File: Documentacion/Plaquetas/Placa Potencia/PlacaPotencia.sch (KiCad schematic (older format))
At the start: 31 parts, among them J1 Conn_01x02_Male, Q1 IRF4905, Q2 IRFZ44N, Q3 IRF4905, Q4 IRFZ44N, Q5 BC337, Q6 BC337, U2 MCP1407, U3 MCP1407

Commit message: Possible layout
Needs some rearenging.
Added kiCAD backup files to ignore list
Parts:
- BORNERA2, BORNERA3: footprint TerminalBlock:TerminalBlock_bornier-2_P5.08mm -> Connector_PinHeader_2.54mm:PinHeader_1x02_P2.54mm_Vertical
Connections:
- net PMOS_CALOR: now also BORNERA3.1 (Pin_1); no longer BORNERA2.2 (Pin_2)
- net PWM_FRIO: now also BORNERA2.2 (Pin_2); no longer BORNERA3.1 (Pin_1)
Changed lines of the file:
@@
 EESchema Schematic File Version 4
+LIBS:PlacaPotencia-cache
 EELAYER 30 0
 EELAYER END
@@
 	1    0    0    -1
 $EndComp
-Text GLabel 9850 1550 2    50   Input ~ 0
+Text GLabel 9950 3100 2    50   Input ~ 0
 PMOS_CALOR
-Text GLabel 9850 1850 2    50   Input ~ 0
-PMOS_FRIO
 $Comp
 L Connector:Screw_Terminal_01x02 BORNERA1
@@
 F 0 "BORNERA2" V 9464 1562 50  0000 R CNN
 F 1 "Screw_Terminal_01x02" V 9373 1562 50  0000 R CNN
-F 2 "TerminalBlock:TerminalBlock_bornier-2_P5.08mm" H 9500 1750 50  0001 C CNN
+F 2 "Connector_PinHeader_2.54mm:PinHeader_1x02_P2.54mm_Vertical" H 9500 1750 50  0001 C CNN
 F 3 "~" H 9500 1750 50  0001 C CNN
 	1    9500 1750
@@
 F 0 "BORNERA3" V 9484 2822 50  0000 R CNN
 F 1 "Screw_Terminal_01x02" V 9393 2822 50  0000 R CNN
-F 2 "TerminalBlock:TerminalBlock_bornier-2_P5.08mm" H 9520 3010 50  0001 C CNN
+F 2 "Connector_PinHeader_2.54mm:PinHeader_1x02_P2.54mm_Vertical" H 9520 3010 50  0001 C CNN
 F 3 "~" H 9520 3010 50  0001 C CNN
 	1    9520 3010
 	-1   0    0    1
 $EndComp
-Text GLabel 9950 3100 2    50   Input ~ 0
-PWM_FRIO
 Text GLabel 9950 2800 2    50   Input ~ 0
 PWM_CALOR
@@
 Wire Wire Line
 	9850 2800 9950 2800
+NoConn ~ 10540 810
+NoConn ~ 10540 910
 $Comp
 L Connector:Conn_01x02_Male J1
@@
 	1    0    0    -1
 $EndComp
-NoConn ~ 10540 810
-NoConn ~ 10540 910
+Text GLabel 9850 1850 2    50   Input ~ 0
+PMOS_FRIO
+Text GLabel 9850 1550 2    50   Input ~ 0
+PWM_FRIO
 $EndSCHEMATC

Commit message: Power PCB Routed
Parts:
- added C_MCP1, C_MCP2: 10n, Capacitor_THT:C_Rect_L7.5mm_W6.5mm_P5.00mm, symbol Device:C
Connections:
- net GND: now also C_MCP1.2, C_MCP2.2
- net VCC: now also C_MCP1.1, C_MCP2.1
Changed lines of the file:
@@
 Text GLabel 9850 1550 2    50   Input ~ 0
 PWM_FRIO
+Text GLabel 9200 3390 1    50   Input ~ 0
+VCC
+$Comp
+L power:GND #PWR0101
+U 1 1 5E2A4616
+P 9200 3860
+F 0 "#PWR0101" H 9200 3610 50  0001 C CNN
+F 1 "GND" H 9205 3687 50  0000 C CNN
+F 2 "" H 9200 3860 50  0001 C CNN
+F 3 "" H 9200 3860 50  0001 C CNN
+	1    9200 3860
+	-1   0    0    -1
+$EndComp
+$Comp
+L Device:C C_MCP1
+U 1 1 5E2A4E3B
+P 8880 3620
+F 0 "C_MCP1" H 8995 3666 50  0000 L CNN
+F 1 "10n" H 8995 3575 50  0000 L CNN
+F 2 "Capacitor_THT:C_Rect_L7.5mm_W6.5mm_P5.00mm" H 8918 3470 50  0001 C CNN
+F 3 "~" H 8880 3620 50  0001 C CNN
+	1    8880 3620
+	1    0    0    -1
+$EndComp
+$Comp
+L Device:C C_MCP2
+U 1 1 5E2A56B2
+P 9520 3620
+F 0 "C_MCP2" H 9635 3666 50  0000 L CNN
+F 1 "10n" H 9635 3575 50  0000 L CNN
+F 2 "Capacitor_THT:C_Rect_L7.5mm_W6.5mm_P5.00mm" H 9558 3470 50  0001 C CNN
+F 3 "~" H 9520 3620 50  0001 C CNN
+	1    9520 3620
+	1    0    0    -1
+$EndComp
+Wire Wire Line
+	8880 3440 8880 3470
+Wire Wire Line
+	9520 3440 9520 3470
+Wire Wire Line
+	8880 3440 9200 3440
+Wire Wire Line
+	8880 3770 8880 3820
+Wire Wire Line
+	8880 3820 9200 3820
+Wire Wire Line
+	9520 3770 9520 3820
+Wire Wire Line
+	9520 3820 9200 3820
+Connection ~ 9200 3820
+Wire Wire Line
+	9200 3820 9200 3860
+Wire Wire Line
+	9200 3390 9200 3440
+Connection ~ 9200 3440
+Wire Wire Line
+	9200 3440 9520 3440
 $EndSCHEMATC

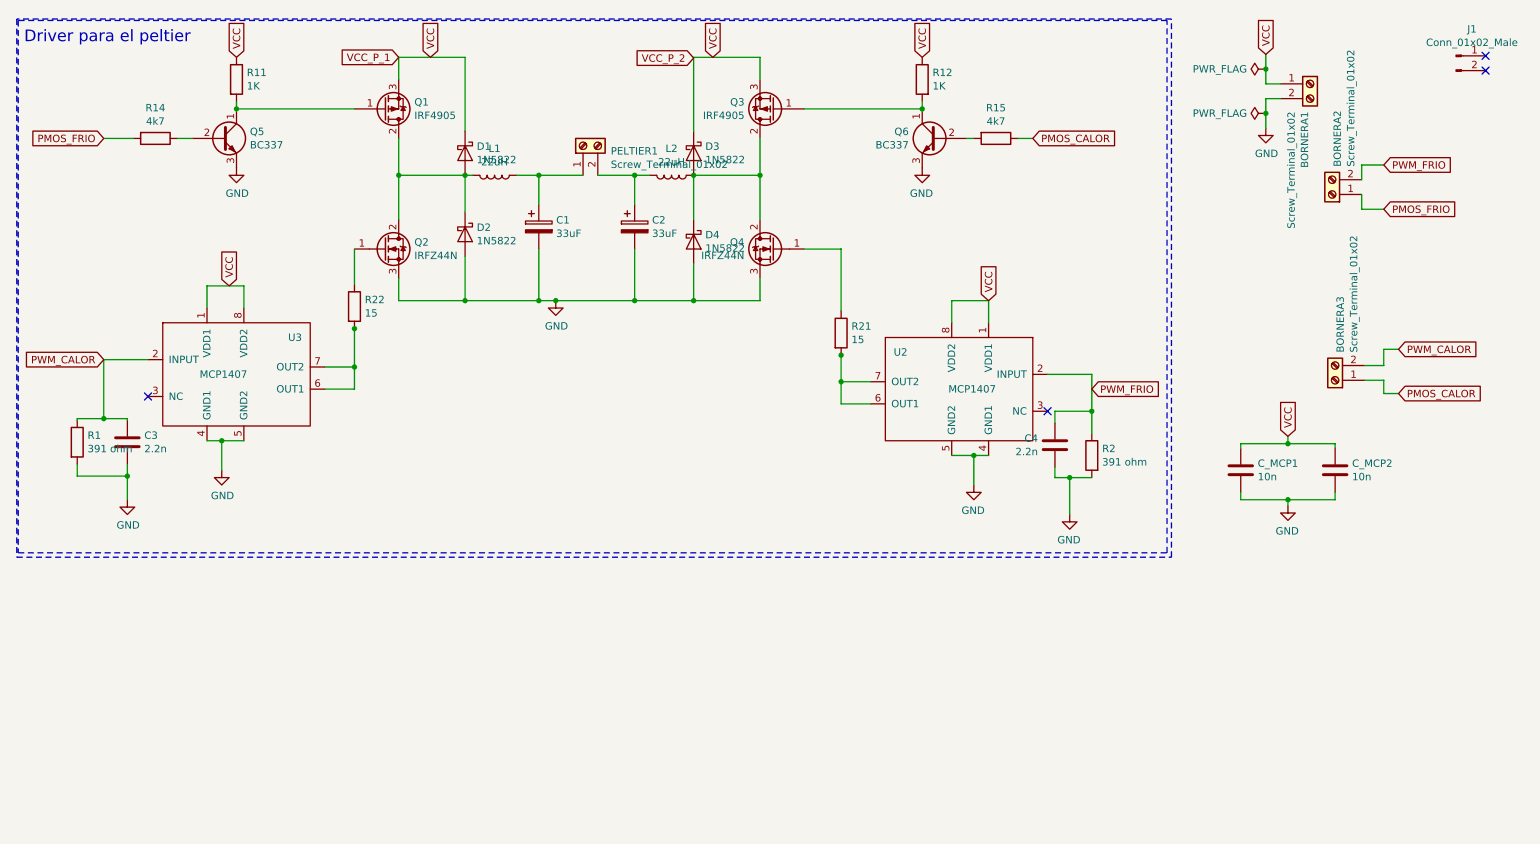
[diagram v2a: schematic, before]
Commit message: Power PCB footprints updated
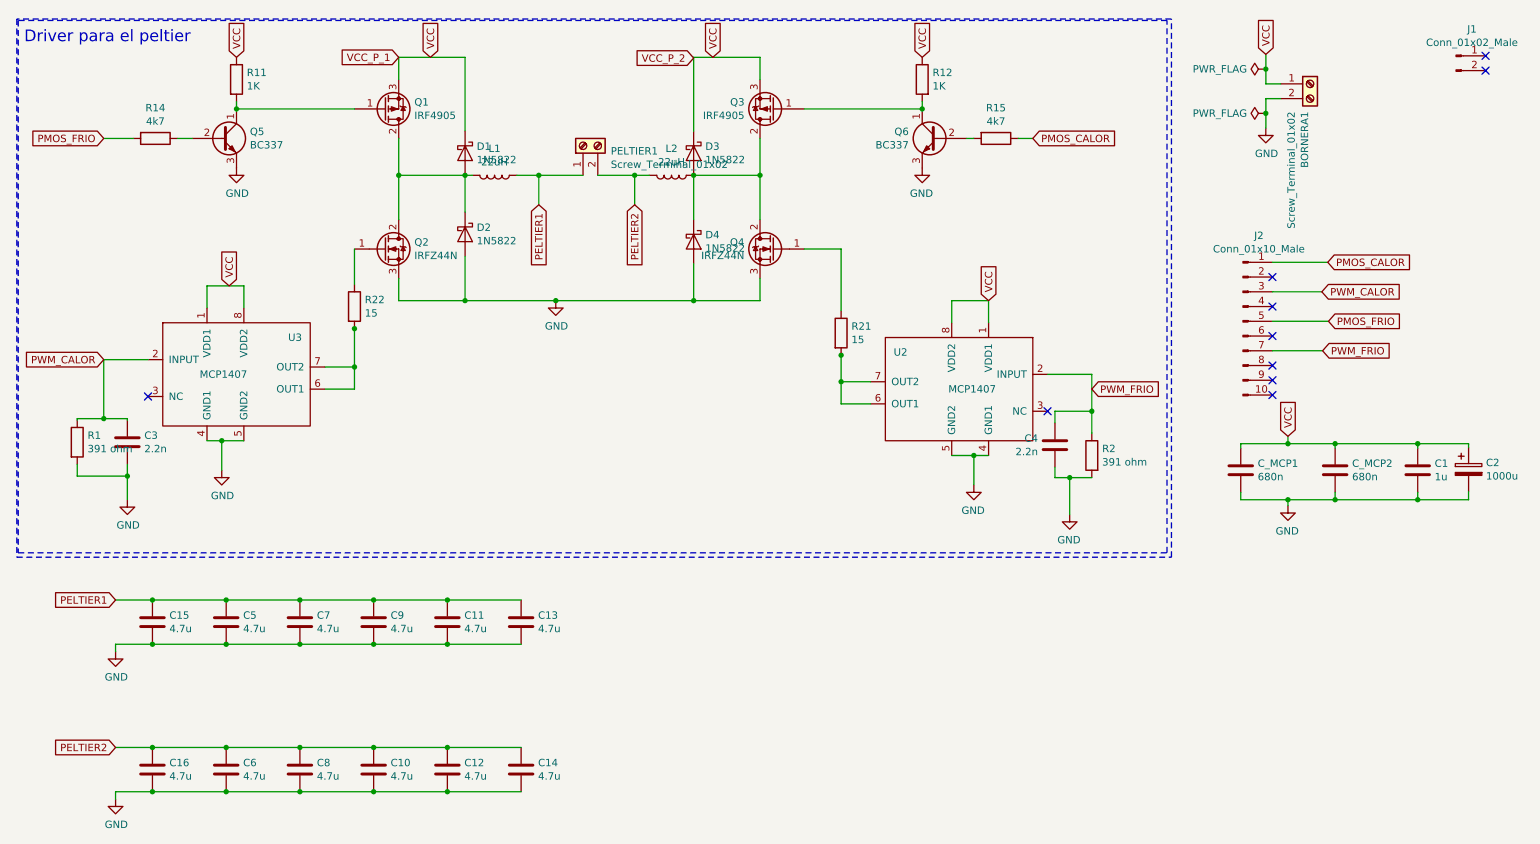
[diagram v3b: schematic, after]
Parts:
- removed BORNERA2, BORNERA3: Screw_Terminal_01x02, Connector_PinHeader_2.54mm:PinHeader_1x02_P2.54mm_Vertical, symbol Connector:Screw_Terminal_01x02
- removed C1: 33uF, Capacitor_THT:CP_Radial_D13.0mm_P7.50mm, symbol Device:CP
- added C1: 1u, Capacitor_THT:C_Rect_L16.5mm_W10.7mm_P15.00mm_MKT, symbol Device:C
- added C10, C11, C12, C13, C14, C15, C16, C5, C6, C7, C8, C9: 4.7u, Capacitor_THT:C_Rect_L29.0mm_W9.1mm_P27.50mm_MKT, symbol Device:C
- added J2: Conn_01x10_Male, Connector_IDC:IDC-Header_2x05_P2.54mm_Vertical, symbol Connector:Conn_01x10_Male
- C2: value 33uF -> 1000u; footprint Capacitor_THT:CP_Radial_D13.0mm_P7.50mm -> Capacitor_THT:CP_Radial_D10.0mm_P5.00mm
- C_MCP1, C_MCP2: value 10n -> 680n; footprint Capacitor_THT:C_Rect_L7.5mm_W6.5mm_P5.00mm -> custom_footprints:C_Rect_L21.5mm_W5.5mm_P20.00mm_MKS4
- R21, R22: footprint Resistor_THT:R_Axial_DIN0204_L3.6mm_D1.6mm_P5.08mm_Horizontal -> Resistor_THT:R_Axial_DIN0411_L9.9mm_D3.6mm_P12.70mm_Horizontal
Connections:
- net GND: now also C1.2, C10.2, C11.2, C12.2, C13.2, C14.2, C15.2, C16.2, C5.2, C6.2, C7.2, C8.2, C9.2
- net PMOS_CALOR: now also J2.1 (Pin_1)
- net PMOS_FRIO: now also J2.5 (Pin_5)
- net PWM_CALOR: now also J2.3 (Pin_3)
- net PWM_FRIO: now also J2.7 (Pin_7)
- net VCC: now also C2.1, C1.1
- net PELTIER1: now reaches L1.1, PELTIER1.1 (Pin_1)
- net PELTIER1: now also C11.1, C13.1, C15.1, C5.1, C7.1, C9.1
- net PELTIER2: now reaches L2.2, PELTIER1.2 (Pin_2)
- net PELTIER2: now also C10.1, C12.1, C14.1, C16.1, C6.1, C8.1; no longer C2.1
- no-connect marks 4 -> 10

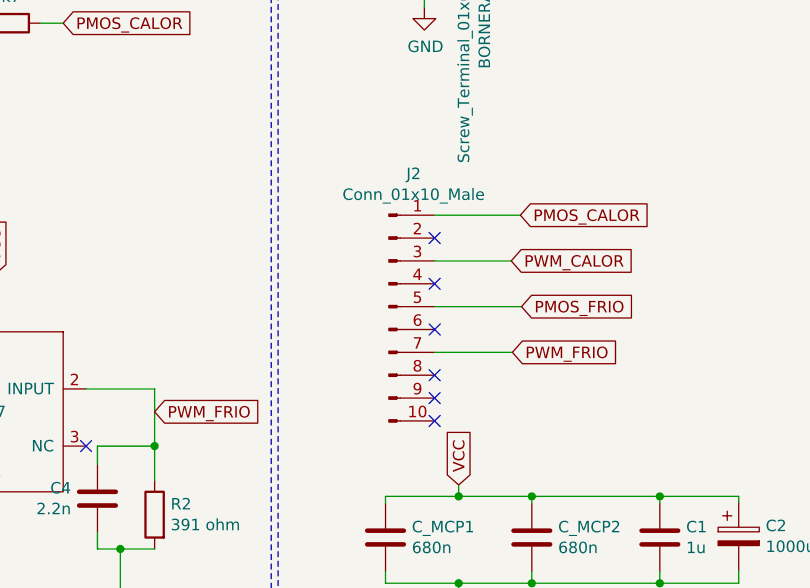
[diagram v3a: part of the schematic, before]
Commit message: Power PCB changed logic connector, widened traces, added mounting holes
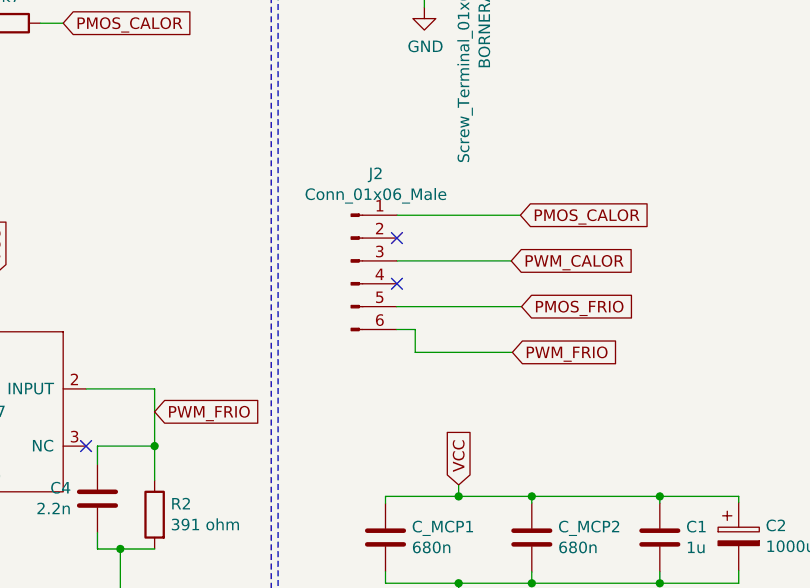
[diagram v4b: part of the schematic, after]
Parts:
- removed J2: Conn_01x10_Male, Connector_IDC:IDC-Header_2x05_P2.54mm_Vertical, symbol Connector:Conn_01x10_Male
- added J2: Conn_01x06_Male, Connector_IDC:IDC-Header_2x03_P2.54mm_Vertical, symbol Connector:Conn_01x06_Male
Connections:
- net PMOS_CALOR: now also J2.1 (Pin_1)
- net PMOS_FRIO: now also J2.5 (Pin_5)
- net PWM_CALOR: now also J2.3 (Pin_3)
- net PWM_FRIO: now also J2.6 (Pin_6)
- no-connect marks 10 -> 6
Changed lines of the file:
@@
 Text GLabel 9435 2810 2    50   Input ~ 0
 PWM_FRIO
-Text GLabel 9200 3390 1    50   Input ~ 0
-VCC
 $Comp
 L power:GND #PWR0101
@@
 Wire Wire Line
 	3500 5800 3000 5800
-$Comp
-L Connector:Conn_01x10_Male J2
-U 1 1 5E3FAAEB
-P 8895 2610
-F 0 "J2" H 9003 3191 50  0000 C CNN
-F 1 "Conn_01x10_Male" H 9003 3100 50  0000 C CNN
-F 2 "Connector_IDC:IDC-Header_2x05_P2.54mm_Vertical" H 8895 2610 50  0001 C CNN
-F 3 "~" H 8895 2610 50  0001 C CNN
-	1    8895 2610
-	1    0    0    -1
-$EndComp
-Wire Wire Line
-	9095 2210 9470 2210
-Wire Wire Line
-	9430 2410 9095 2410
-Wire Wire Line
-	9475 2610 9095 2610
-Wire Wire Line
-	9435 2810 9095 2810
-NoConn ~ 9095 2310
-NoConn ~ 9095 2510
-NoConn ~ 9095 2710
-NoConn ~ 9095 2910
-NoConn ~ 9095 3010
-NoConn ~ 9095 3110
+NoConn ~ 8930 2310
+NoConn ~ 8930 2510
+$Comp
+L Connector:Conn_01x06_Male J2
+U 1 1 5E3E38C6
+P 8730 2410
+F 0 "J2" H 8838 2791 50  0000 C CNN
+F 1 "Conn_01x06_Male" H 8838 2700 50  0000 C CNN
+F 2 "Connector_IDC:IDC-Header_2x03_P2.54mm_Vertical" H 8730 2410 50  0001 C CNN
+F 3 "~" H 8730 2410 50  0001 C CNN
+	1    8730 2410
+	1    0    0    -1
+$EndComp
+Wire Wire Line
+	8930 2410 9430 2410
+Wire Wire Line
+	8930 2710 9010 2710
+Wire Wire Line
+	9010 2710 9010 2810
+Wire Wire Line
+	9010 2810 9435 2810
+Wire Wire Line
+	8930 2610 9475 2610
+Wire Wire Line
+	8930 2210 9470 2210
+Text GLabel 9200 3390 1    50   Input ~ 0
+VCC
 $EndSCHEMATC
